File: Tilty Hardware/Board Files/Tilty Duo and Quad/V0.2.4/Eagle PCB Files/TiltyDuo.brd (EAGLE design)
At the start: 38.1 x 50.8 mm, 45 parts, among them U1 TEENSY_3.0_OUTER-PINS28-DIP_S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, U2 HC-09_BREAKOUT, U3 MPL3115A2LGA8, U4 LM2931, U5 MPU-6050, U6 HMC5883LSMD, U7 SPI_FLASH-X25XXSMD

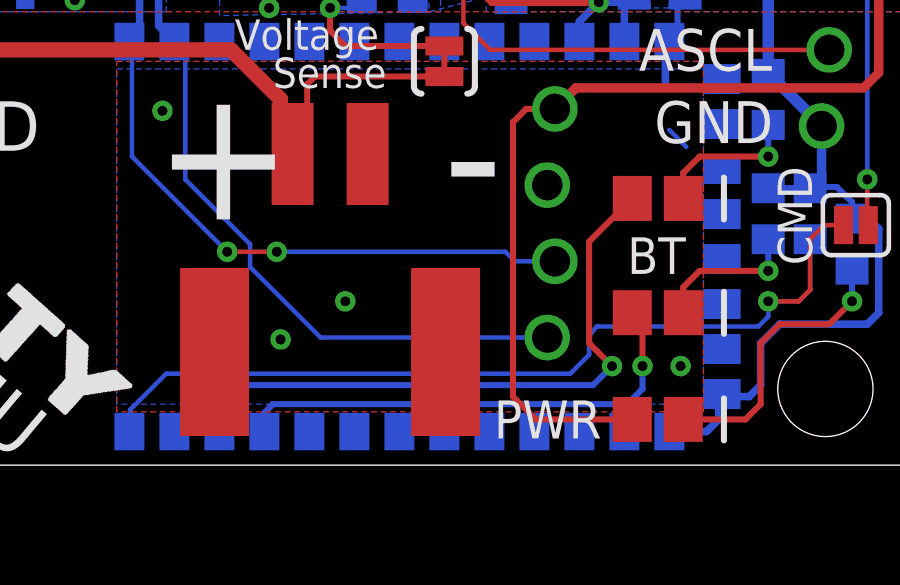
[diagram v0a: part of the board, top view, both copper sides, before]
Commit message: Tweaked LED order on Duo/Quad, added lots of memory testing (libraries to come soon)
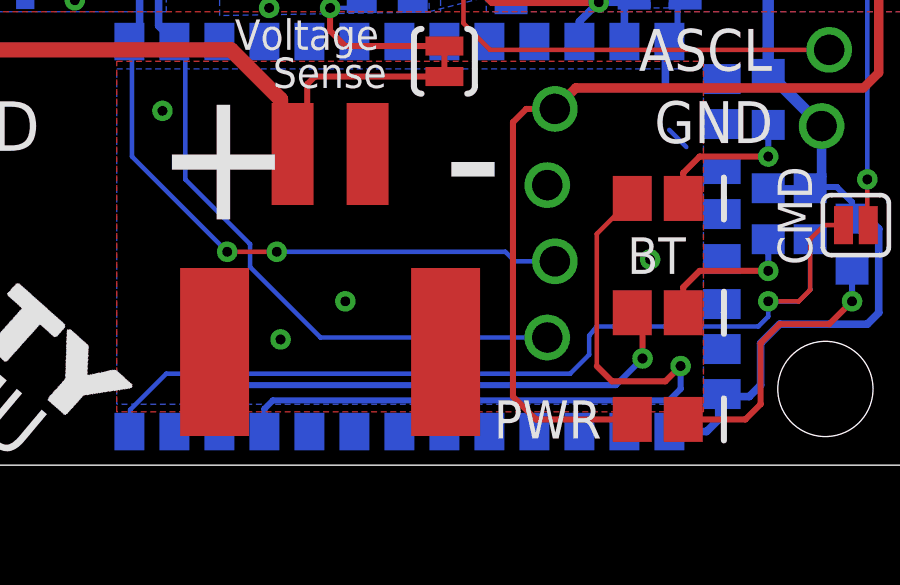
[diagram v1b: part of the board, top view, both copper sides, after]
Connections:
- removed net RED_LED: D1.1, U2.P$32
- new net N$14: D1.1, U2.P$31
- net YEL_LED: now also U2.P$32; no longer U2.P$31
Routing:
- net N$14: track 0.00 -> 25.0 mm, vias 0 -> 1
- net RED_LED: track 20.9 -> 0.00 mm, vias 1 -> 0
- net YEL_LED: track 16.2 -> 17.5 mm
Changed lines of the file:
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@@
 <?xml version="1.0" encoding="utf-8"?>
 <!DOCTYPE eagle SYSTEM "eagle.dtd">
-<eagle version="6.4">
+<eagle version="6.5.0">
 <drawing>
 <settings>
@@
 <setting verticaltext="up"/>
 </settings>
-<grid distance="0.05" unitdist="inch" unit="inch" style="lines" multiple="1" display="yes" altdistance="0.005" altunitdist="inch" altunit="inch"/>
+<grid distance="0.01" unitdist="inch" unit="inch" style="lines" multiple="1" display="yes" altdistance="0.005" altunitdist="inch" altunit="inch"/>
 <layers>
 <layer number="1" name="Top" color="4" fill="1" visible="yes" active="yes"/>
@@
 <wire x1="33.02" y1="2.286" x2="32.194" y2="2.286" width="0.254" layer="16"/>
 <wire x1="32.194" y1="2.286" x2="32.11" y2="2.37" width="0.254" layer="16"/>
-<via x="30.734" y="3.302" extent="1-16" drill="0.3302"/>
+<via x="29.718" y="6.858" extent="1-16" drill="0.3302"/>
 <contactref element="U1" pad="P$16"/>
 <wire x1="20.32" y1="23.38" x2="20.955" y2="22.86" width="0.1524" layer="16"/>
@@
 </signal>
 <signal name="YEL_LED">
-<contactref element="U2" pad="P$31"/>
 <contactref element="D3" pad="1"/>
-<wire x1="16.86" y1="1.12" x2="16.86" y2="1.747" width="0.2032" layer="16"/>
-<wire x1="28.956" y1="2.032" x2="17.145" y2="2.032" width="0.2032" layer="16"/>
-<wire x1="17.145" y1="2.032" x2="16.86" y2="1.747" width="0.2032" layer="16"/>
-<via x="29.464" y="3.302" extent="1-16" drill="0.3302"/>
-<wire x1="28.956" y1="2.032" x2="29.464" y2="2.54" width="0.2032" layer="16"/>
-<wire x1="29.464" y1="2.54" x2="29.464" y2="3.302" width="0.2032" layer="16"/>
-<wire x1="29.464" y1="3.302" x2="29.464" y2="4.738" width="0.2032" layer="1"/>
+<via x="29.464" y="3.556" extent="1-16" drill="0.3302"/>
+<wire x1="29.464" y1="3.556" x2="29.464" y2="4.738" width="0.2032" layer="1"/>
 <wire x1="29.464" y1="4.738" x2="29.122" y2="5.08" width="0.2032" layer="1"/>
+<contactref element="U2" pad="P$32"/>
+<wire x1="15.36" y1="1.12" x2="15.36" y2="2.279" width="0.2032" layer="16"/>
+<wire x1="15.36" y1="2.279" x2="15.748" y2="2.667" width="0.2032" layer="16"/>
+<wire x1="15.748" y1="2.667" x2="28.575" y2="2.667" width="0.2032" layer="16"/>
+<wire x1="28.575" y1="2.667" x2="29.464" y2="3.556" width="0.2032" layer="16"/>
 </signal>
 <signal name="N$24">
@@
 <wire x1="35.687" y1="4.699" x2="36.449" y2="5.461" width="0.2032" layer="1"/>
 </signal>
-<signal name="RED_LED">
-<via x="28.448" y="3.302" extent="1-16" drill="0.3302"/>
-<contactref element="U2" pad="P$32"/>
-<contactref element="D1" pad="1"/>
-<wire x1="15.36" y1="1.12" x2="15.36" y2="1.771" width="0.2032" layer="16"/>
-<wire x1="15.36" y1="1.771" x2="16.256" y2="2.667" width="0.2032" layer="16"/>
-<wire x1="16.256" y1="2.667" x2="27.813" y2="2.667" width="0.2032" layer="16"/>
-<wire x1="28.448" y1="3.302" x2="27.686" y2="4.064" width="0.2032" layer="1"/>
-<wire x1="27.686" y1="4.064" x2="27.686" y2="7.454" width="0.2032" layer="1"/>
-<wire x1="27.686" y1="7.454" x2="29.122" y2="8.89" width="0.2032" layer="1"/>
-<wire x1="27.813" y1="2.667" x2="28.448" y2="3.302" width="0.2032" layer="16"/>
-</signal>
 <signal name="N$9">
 <contactref element="R5" pad="1"/>
@@
 <wire x1="26.67" y1="17.78" x2="26.67" y2="18.923" width="0.2032" layer="16"/>
 </signal>
+<signal name="N$14">
+<contactref element="D1" pad="1"/>
+<contactref element="U2" pad="P$31"/>
+<via x="30.734" y="3.302" extent="1-16" drill="0.3302"/>
+<wire x1="30.734" y1="3.302" x2="30.226" y2="2.794" width="0.2032" layer="1"/>
+<wire x1="30.226" y1="2.794" x2="28.448" y2="2.794" width="0.2032" layer="1"/>
+<wire x1="28.448" y1="2.794" x2="27.94" y2="3.302" width="0.2032" layer="1"/>
+<wire x1="27.94" y1="3.302" x2="27.94" y2="7.708" width="0.1524" layer="1"/>
+<wire x1="27.94" y1="7.708" x2="29.122" y2="8.89" width="0.1524" layer="1"/>
+<wire x1="16.86" y1="1.12" x2="16.86" y2="1.874" width="0.2032" layer="16"/>
+<wire x1="16.86" y1="1.874" x2="17.145" y2="2.159" width="0.2032" layer="16"/>
+<wire x1="17.145" y1="2.159" x2="30.353" y2="2.159" width="0.2032" layer="16"/>
+<wire x1="30.353" y1="2.159" x2="30.734" y2="2.54" width="0.2032" layer="16"/>
+<wire x1="30.734" y1="2.54" x2="30.734" y2="3.302" width="0.2032" layer="16"/>
+</signal>
 </signals>
+<errors>
+</errors>
 </board>
 </drawing>

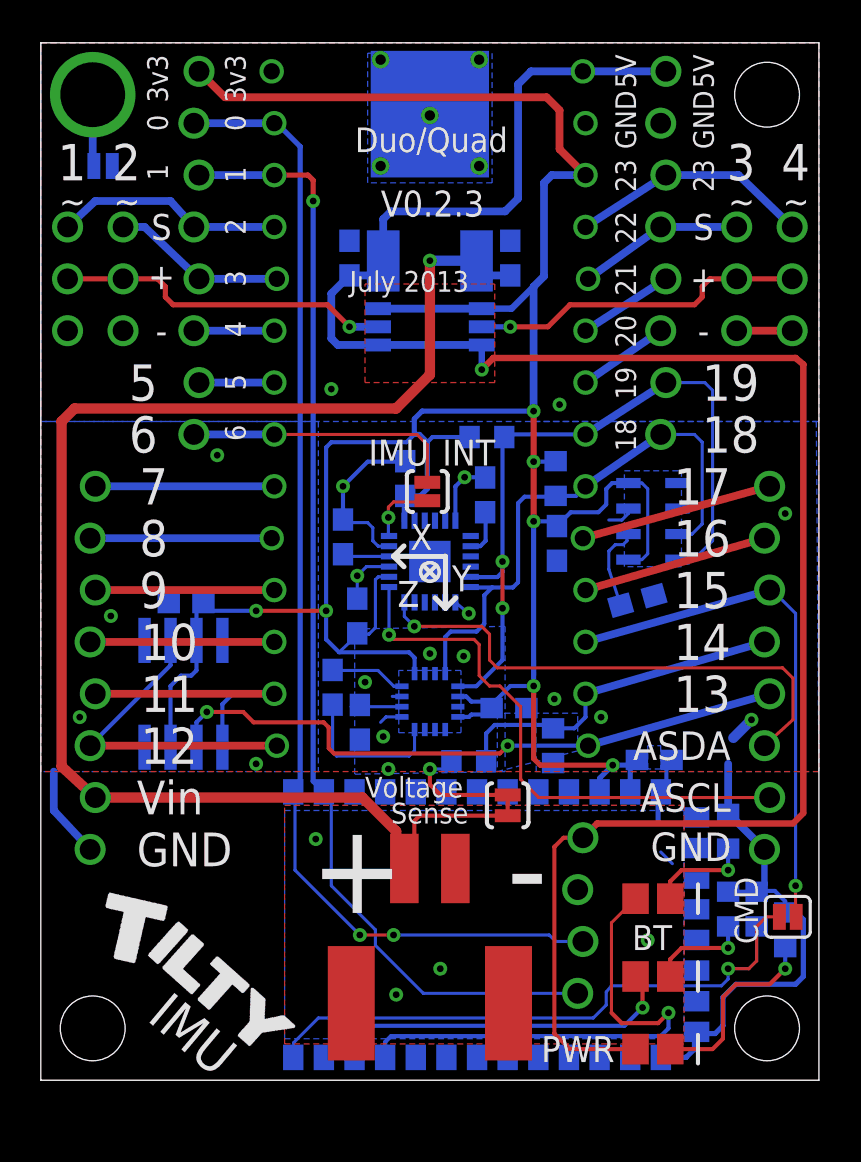
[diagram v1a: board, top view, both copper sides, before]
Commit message: Updated Altimeter library to take data pointers as well as return data
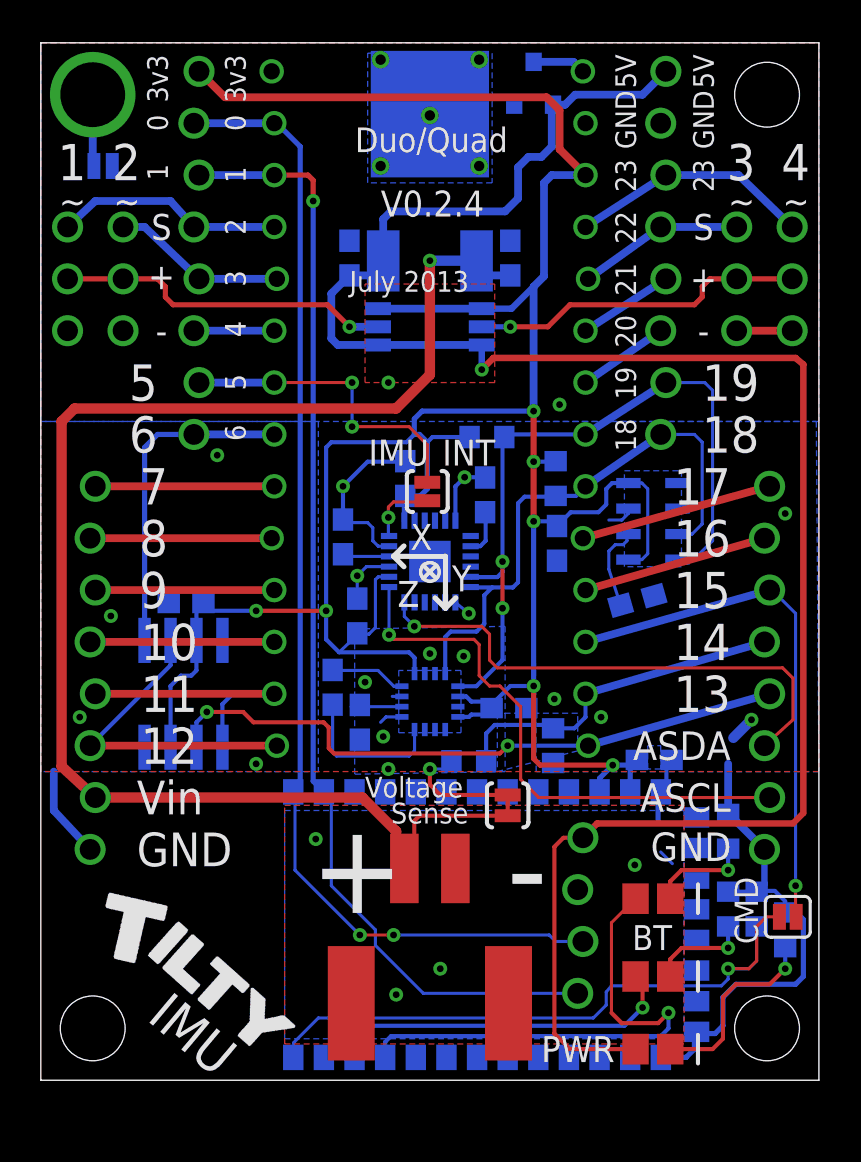
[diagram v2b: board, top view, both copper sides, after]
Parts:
- added D4: (no value), SparkFun-DiscreteSemi:SOT23-3
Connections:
- new net N$15: D4.3, U1.P$15
- net 5V: now also D4.1; no longer U1.P$15
- net CS: now also JP1.1, U1.P$8; no longer JP2.5, U1.P$12
- net MPU_INT: now also JP1.2, U1.P$7; no longer JP1.1, U1.P$8
- net N$8: now also JP2.5, U1.P$12; no longer JP1.2, U1.P$7
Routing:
- net N$8: track 3.68 -> 9.02 mm
- net CS: track 11.7 -> 16.2 mm
- net N$15: track 0.00 -> 2.61 mm
- net MPU_INT: track 13.5 -> 15.5 mm, vias 0 -> 2
- net 5V: track 101.2 -> 100.0 mm
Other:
- board text added: "V0.2.4"
- board text removed: "V0.2.3"
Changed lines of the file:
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@@
 <layer number="23" name="tOrigins" color="15" fill="1" visible="yes" active="yes"/>
 <layer number="24" name="bOrigins" color="15" fill="1" visible="yes" active="yes"/>
-<layer number="25" name="tNames" color="14" fill="1" visible="no" active="yes"/>
-<layer number="26" name="bNames" color="6" fill="1" visible="no" active="yes"/>
+<layer number="25" name="tNames" color="14" fill="1" visible="yes" active="yes"/>
+<layer number="26" name="bNames" color="6" fill="1" visible="yes" active="yes"/>
 <layer number="27" name="tValues" color="7" fill="1" visible="no" active="yes"/>
 <layer number="28" name="bValues" color="7" fill="1" visible="no" active="yes"/>
@@
 <layer number="49" name="Reference" color="7" fill="1" visible="no" active="yes"/>
 <layer number="50" name="dxf" color="7" fill="1" visible="no" active="no"/>
-<layer number="51" name="tDocu" color="6" fill="1" visible="yes" active="yes"/>
-<layer number="52" name="bDocu" color="7" fill="1" visible="no" active="yes"/>
+<layer number="51" name="tDocu" color="15" fill="1" visible="yes" active="yes"/>
+<layer number="52" name="bDocu" color="7" fill="1" visible="yes" active="yes"/>
 <layer number="53" name="tGND_GNDA" color="7" fill="9" visible="no" active="no"/>
 <layer number="54" name="bGND_GNDA" color="1" fill="9" visible="no" active="no"/>
@@
 <text x="9.525" y="47.879" size="1.016" layer="25" ratio="12" rot="R90" align="center-left">3v3</text>
 <text x="19.12359375" y="46.051375" size="1.2065" layer="25" ratio="12" align="center">Duo/Quad</text>
-<text x="19.177" y="42.926" size="1.27" layer="25" ratio="12" align="center">V0.2.3</text>
+<text x="19.177" y="42.926" size="1.27" layer="25" ratio="12" align="center">V0.2.4</text>
 <text x="28.956" y="6.985" size="1.2192" layer="25" ratio="12" align="center-left">BT</text>
 <text x="4.445" y="10.16" size="1.016" layer="26" ratio="10" rot="MR75" align="center-left">GND</text>
@@
 <attribute name="VALUE" x="37.5258" y="9.652" size="0.4064" layer="27" rot="R180"/>
 </element>
+<element name="D4" library="SparkFun-DiscreteSemi" package="SOT23-3" value="" x="24.13" y="48.768" smashed="yes" rot="MR0">
+<attribute name="VALUE" x="25.146" y="48.5775" size="0.4064" layer="28" rot="MR0"/>
+</element>
 </elements>
 <signals>
@@
 <via x="25.4" y="33.0835" extent="1-16" drill="0.3302"/>
 <via x="8.636" y="30.607" extent="1-16" drill="0.3302"/>
-<via x="14.224" y="33.8455" extent="1-16" drill="0.3302"/>
+<via x="17.018" y="34.163" extent="1-16" drill="0.3302"/>
 <polygon width="0.1524" layer="16" isolate="0.2032" orphans="yes">
 <vertex x="15.367" y="22.098"/>
@@
 <wire x1="33.02" y1="2.286" x2="32.194" y2="2.286" width="0.254" layer="16"/>
 <wire x1="32.194" y1="2.286" x2="32.11" y2="2.37" width="0.254" layer="16"/>
-<via x="29.718" y="6.858" extent="1-16" drill="0.3302"/>
+<via x="29.083" y="10.541" extent="1-16" drill="0.3302"/>
 <contactref element="U1" pad="P$16"/>
 <wire x1="20.32" y1="23.38" x2="20.955" y2="22.86" width="0.1524" layer="16"/>
@@
 <contactref element="U1" pad="P$9"/>
 <contactref element="JP2" pad="8"/>
-<wire x1="11.43" y1="29.083" x2="2.667" y2="29.083" width="0.381" layer="16"/>
+<wire x1="11.43" y1="29.083" x2="2.667" y2="29.083" width="0.381" layer="1"/>
 </signal>
 <signal name="TX3">
 <contactref element="U1" pad="P$10"/>
 <contactref element="JP2" pad="7"/>
-<wire x1="2.413" y1="26.543" x2="11.303" y2="26.543" width="0.381" layer="16"/>
+<wire x1="2.413" y1="26.543" x2="11.303" y2="26.543" width="0.381" layer="1"/>
 </signal>
 <signal name="MPU_INT">
 <contactref element="MPU_INT" pad="1"/>
-<contactref element="U1" pad="P$8"/>
-<contactref element="JP1" pad="1"/>
-<wire x1="11.43" y1="31.623" x2="7.493" y2="31.623" width="0.381" layer="16"/>
-<wire x1="11.43" y1="31.623" x2="18.415" y2="31.623" width="0.1524" layer="1"/>
-<wire x1="18.415" y1="31.623" x2="18.923" y2="31.115" width="0.1524" layer="1"/>
+<wire x1="18.034" y1="32.004" x2="18.923" y2="31.115" width="0.1524" layer="1"/>
 <wire x1="18.923" y1="31.115" x2="18.923" y2="29.279" width="0.1524" layer="1"/>
+<contactref element="U1" pad="P$7"/>
+<contactref element="JP1" pad="2"/>
+<wire x1="11.43" y1="34.163" x2="7.747" y2="34.163" width="0.381" layer="16"/>
+<via x="15.24" y="32.004" extent="1-16" drill="0.3302"/>
+<via x="15.24" y="34.163" extent="1-16" drill="0.3302"/>
+<wire x1="18.034" y1="32.004" x2="15.24" y2="32.004" width="0.1524" layer="1"/>
+<wire x1="15.24" y1="32.004" x2="15.24" y2="34.163" width="0.1524" layer="16"/>
+<wire x1="15.24" y1="34.163" x2="11.43" y2="34.163" width="0.1524" layer="1"/>
 </signal>
 <signal name="VBATT">
@@
 <contactref element="U4" pad="P$3"/>
 <contactref element="C5" pad="1"/>
-<contactref element="U1" pad="P$15"/>
-<contactref element="JP5" pad="8"/>
-<wire x1="26.543" y1="49.403" x2="30.607" y2="49.403" width="0.381" layer="16"/>
 <contactref element="JP9" pad="4"/>
 <wire x1="37.338" y1="13.081" x2="37.338" y2="35.052" width="0.3175" layer="1"/>
@@
 <wire x1="15.113" y1="39.409" x2="16.764" y2="39.409" width="0.381" layer="16"/>
 <wire x1="16.764" y1="39.409" x2="16.764" y2="40.1193" width="0.381" layer="16"/>
-<wire x1="26.543" y1="49.403" x2="24.003" y2="49.403" width="0.381" layer="16"/>
-<wire x1="24.003" y1="49.403" x2="23.368" y2="48.768" width="0.381" layer="16"/>
 <wire x1="22.733" y1="42.545" x2="17.145" y2="42.545" width="0.381" layer="16"/>
 <wire x1="22.733" y1="42.545" x2="23.368" y2="43.18" width="0.381" layer="16"/>
-<wire x1="23.368" y1="43.18" x2="23.368" y2="48.768" width="0.381" layer="16"/>
 <wire x1="17.145" y1="42.545" x2="16.764" y2="42.164" width="0.381" layer="16"/>
 <wire x1="16.764" y1="42.164" x2="16.764" y2="40.1193" width="0.381" layer="16"/>
+<contactref element="D4" pad="1"/>
+<contactref element="JP5" pad="8"/>
+<wire x1="23.368" y1="43.18" x2="23.368" y2="44.704" width="0.381" layer="16"/>
+<wire x1="23.368" y1="44.704" x2="23.876" y2="45.212" width="0.381" layer="16"/>
+<wire x1="23.876" y1="45.212" x2="24.511" y2="45.212" width="0.381" layer="16"/>
+<wire x1="24.511" y1="45.212" x2="25.019" y2="45.72" width="0.381" layer="16"/>
+<wire x1="25.019" y1="45.72" x2="25.019" y2="47.707" width="0.381" layer="16"/>
+<wire x1="25.019" y1="47.707" x2="25.08" y2="47.768" width="0.381" layer="16"/>
+<wire x1="25.08" y1="47.768" x2="25.67" y2="47.768" width="0.381" layer="16"/>
+<wire x1="25.67" y1="47.768" x2="26.162" y2="48.26" width="0.381" layer="16"/>
+<wire x1="26.162" y1="48.26" x2="29.464" y2="48.26" width="0.381" layer="16"/>
+<wire x1="29.464" y1="48.26" x2="30.607" y2="49.403" width="0.381" layer="16"/>
 </signal>
 <signal name="N$7">
@@
 <contactref element="JP1" pad="3"/>
 <wire x1="11.43" y1="36.703" x2="7.493" y2="36.703" width="0.381" layer="16"/>
-</signal>
-<signal name="N$8">
-<contactref element="U1" pad="P$7"/>
-<contactref element="JP1" pad="2"/>
-<wire x1="11.43" y1="34.163" x2="7.747" y2="34.163" width="0.381" layer="16"/>
 </signal>
 <signal name="N$12">
@@
 <signal name="CS">
 <contactref element="U7" pad="1"/>
-<contactref element="U1" pad="P$12"/>
-<contactref element="JP2" pad="5"/>
-<wire x1="2.413" y1="21.463" x2="11.43" y2="21.463" width="0.381" layer="1"/>
-<wire x1="2.413" y1="21.463" x2="5.0038" y2="21.463" width="0.2032" layer="16"/>
 <wire x1="5.0038" y1="21.463" x2="5.08" y2="21.5392" width="0.2032" layer="16"/>
+<contactref element="U1" pad="P$8"/>
+<contactref element="JP1" pad="1"/>
+<wire x1="11.43" y1="31.623" x2="7.493" y2="31.623" width="0.381" layer="16"/>
+<wire x1="5.08" y1="21.5392" x2="5.08" y2="30.988" width="0.254" layer="16"/>
+<wire x1="5.08" y1="30.988" x2="5.715" y2="31.623" width="0.254" layer="16"/>
+<wire x1="5.715" y1="31.623" x2="7.493" y2="31.623" width="0.254" layer="16"/>
 </signal>
 <signal name="SCK">
@@
 <wire x1="30.734" y1="2.54" x2="30.734" y2="3.302" width="0.2032" layer="16"/>
 </signal>
+<signal name="N$8">
+<contactref element="JP2" pad="5"/>
+<contactref element="U1" pad="P$12"/>
+<wire x1="2.413" y1="21.463" x2="11.43" y2="21.463" width="0.381" layer="1"/>
+</signal>
+<signal name="N$15">
+<contactref element="D4" pad="3"/>
+<contactref element="U1" pad="P$15"/>
+<wire x1="24.13" y1="49.868" x2="26.078" y2="49.868" width="0.381" layer="16"/>
+<wire x1="26.078" y1="49.868" x2="26.543" y2="49.403" width="0.381" layer="16"/>
+</signal>
 </signals>

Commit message: Updated Tilty Duo/Quad PCB and TiltyIMU software library
PCB: Added circuit protection
Software: Fixed conflicts with duplicate file names
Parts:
- added D5: (no value), SparkFun-DiscreteSemi:SOT23-3
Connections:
- net GND: now also D5.1
- net TEENSY_3V3: now also D5.3
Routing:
- net TEENSY_3V3: track 143.5 -> 151.4 mm
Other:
- board text added: "Aug 2013"
- board text removed: "July 2013"
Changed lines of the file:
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@@
 <rectangle x1="12.4457375" y1="2.670165625" x2="12.46605625" y2="2.690484375" layer="25" rot="R285"/>
 <text x="5.140959375" y="2.96671875" size="1.905" layer="25" font="vector" ratio="17" rot="R320">IMU</text>
-<text x="15.113" y="38.608" size="1.016" layer="25" font="vector" ratio="12">July 2013</text>
+<text x="15.367" y="38.608" size="1.016" layer="25" font="vector" ratio="12">Aug 2013</text>
 <text x="5.7785" y="41.783" size="1.27" layer="26" ratio="15" rot="MR0" align="center">S</text>
 <text x="5.7785" y="39.37" size="1.27" layer="26" ratio="15" rot="MR0" align="center">+</text>
@@
 <attribute name="VALUE" x="25.146" y="48.5775" size="0.4064" layer="28" rot="MR0"/>
 </element>
+<element name="D5" library="SparkFun-DiscreteSemi" package="SOT23-3" value="" x="13.97" y="48.768" smashed="yes" rot="MR0">
+<attribute name="VALUE" x="14.986" y="48.5775" size="0.4064" layer="28" rot="MR0"/>
+<attribute name="PART#" value="BZX84C3V3LT1GOSCT-ND" x="13.97" y="48.768" size="1.778" layer="28" rot="MR0" display="off"/>
+</element>
 </elements>
 <signals>
@@
 <via x="19.05" y="20.8915" extent="1-16" drill="0.3302"/>
 <via x="36.449" y="27.7495" extent="1-16" drill="0.3302"/>
+<contactref element="D5" pad="1"/>
 </signal>
 <signal name="SCL" class="4">
@@
 <wire x1="24.638" y1="43.942" x2="24.638" y2="39.37" width="0.381" layer="16"/>
 <wire x1="24.638" y1="39.37" x2="24.13" y2="38.862" width="0.381" layer="16"/>
+<contactref element="D5" pad="3"/>
+<wire x1="13.97" y1="49.868" x2="13.97" y2="49.022" width="0.381" layer="16"/>
+<wire x1="13.97" y1="49.022" x2="13.716" y2="48.768" width="0.381" layer="16"/>
+<wire x1="13.716" y1="48.768" x2="12.319" y2="48.768" width="0.381" layer="16"/>
+<wire x1="12.319" y1="48.768" x2="11.684" y2="48.133" width="0.381" layer="16"/>
+<wire x1="11.684" y1="48.133" x2="9.017" y2="48.133" width="0.381" layer="16"/>
+<wire x1="9.017" y1="48.133" x2="7.747" y2="49.403" width="0.381" layer="16"/>
 </signal>
 <signal name="5V">
